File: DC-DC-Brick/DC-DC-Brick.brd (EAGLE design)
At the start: 48.3 x 73.7 mm, 20 parts

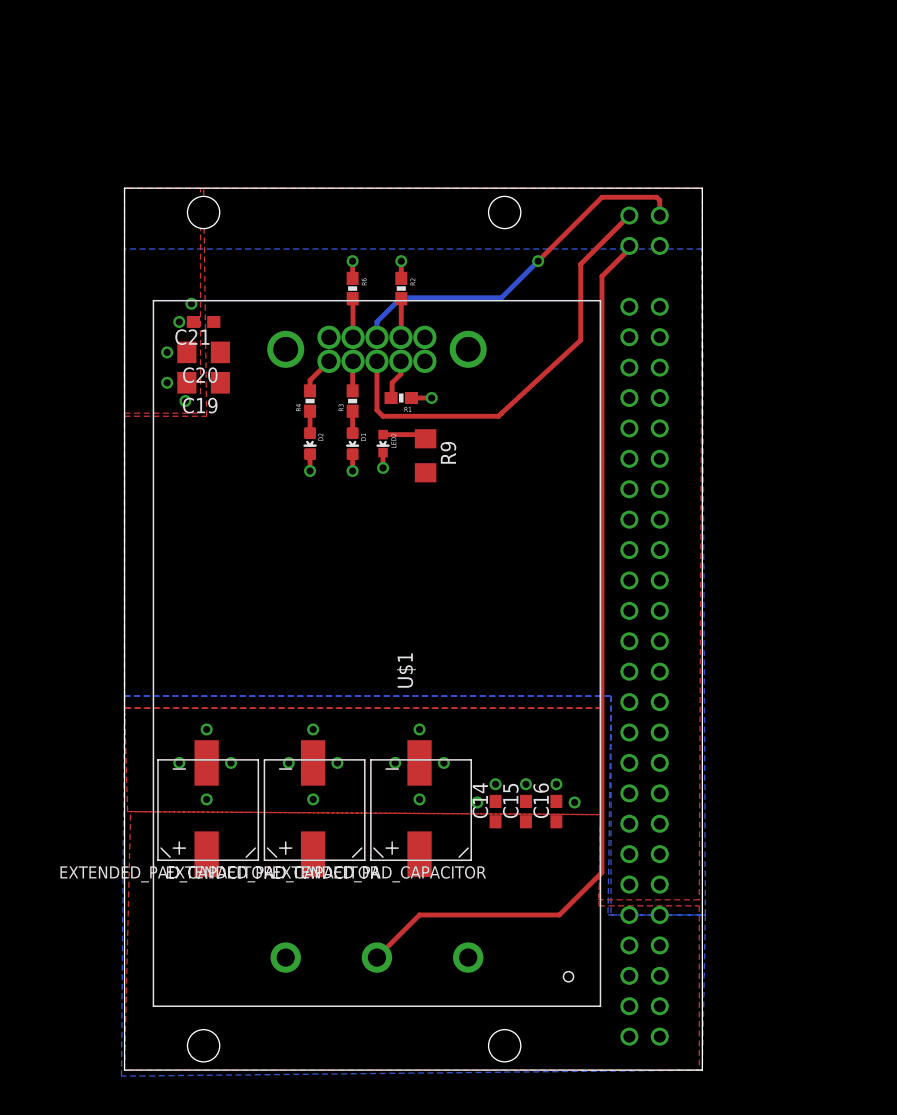
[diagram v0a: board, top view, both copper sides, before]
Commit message: Fixed some routing and added resistor
Added resistor between ON/OFF pin and V-. The resistor's value is not
necessarily the value we will end up using.
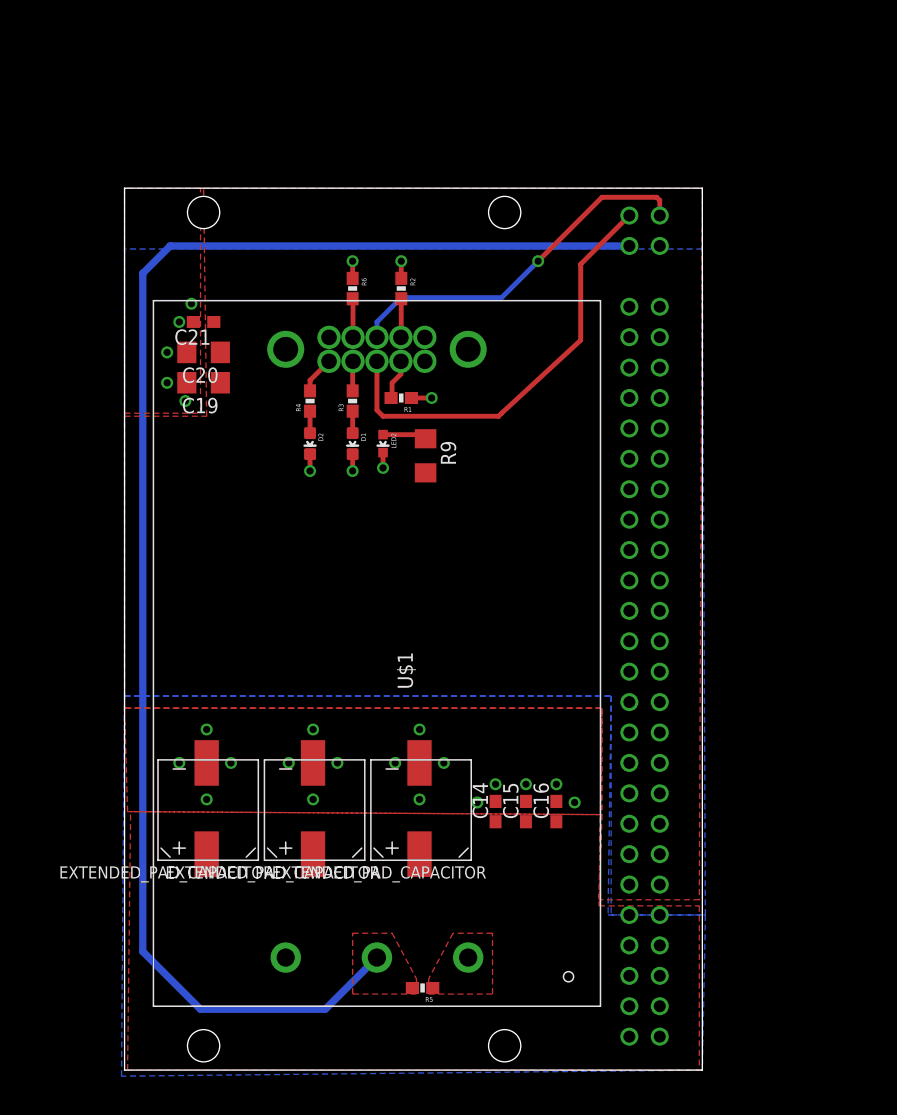
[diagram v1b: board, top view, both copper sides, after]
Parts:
- added R5: 220, SparkFun-Resistors:0603-RES
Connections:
- removed net N$9: U$1.2, U$3.P$51
- new net ON/OFF: R5.2, U$1.2, U$3.P$51
- net V-: now also R5.1
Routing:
- net ON/OFF: track 0.00 -> 121.6 mm
- net N$9: track 75.0 -> 0.00 mm
- added copper zone on layer 1, net ON/OFF
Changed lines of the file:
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@@
 <element name="U$1" library="PowerComponents" package="BRICK_DC-DC_CONVERTER" value="BRICK_DC-DC_CONVERTER" x="21.082" y="34.798" rot="R90"/>
 <element name="U$3" library="MotherboardParts" package="POWER-BRICK-CONNECTOR" value="POWER-BRICK-CONNECTOR" x="43.434" y="37.084"/>
+<element name="R5" library="SparkFun-Resistors" package="0603-RES" value="220" x="24.892" y="6.858" rot="R180">
+<attribute name="PROD_ID" value="RES-07856" x="24.892" y="6.858" size="1.778" layer="27" rot="R180" display="off"/>
+</element>
 </elements>
 <signals>
@@
 <contactref element="C22V6" pad="P$3"/>
 <contactref element="U$1" pad="1"/>
-<polygon width="0.4064" layer="1">
-<vertex x="0" y="0"/>
+<polygon width="0.4064" layer="1" rank="2">
+<vertex x="0.254" y="0"/>
 <vertex x="0.508" y="21.59"/>
 <vertex x="39.878" y="21.336"/>
@@
 <contactref element="U$3" pad="P$8"/>
 <contactref element="U$3" pad="P$9"/>
+<contactref element="R5" pad="1"/>
+<polygon width="0.6096" layer="1">
+<vertex x="27.432" y="11.43"/>
+<vertex x="25.4" y="7.62"/>
+<vertex x="25.4" y="6.35"/>
+<vertex x="30.734" y="6.35"/>
+<vertex x="30.734" y="11.43"/>
+</polygon>
 </signal>
 <signal name="N$12">
@@
 </polygon>
 </signal>
-<signal name="N$9">
+<signal name="ON/OFF">
 <contactref element="U$1" pad="2"/>
 <contactref element="U$3" pad="P$51"/>
-<wire x1="21.082" y1="9.398" x2="24.638" y2="12.954" width="0.4064" layer="1"/>
-<wire x1="24.638" y1="12.954" x2="36.322" y2="12.954" width="0.4064" layer="1"/>
-<wire x1="36.322" y1="12.954" x2="39.878" y2="16.51" width="0.4064" layer="1"/>
-<wire x1="39.878" y1="16.51" x2="39.878" y2="66.294" width="0.4064" layer="1"/>
-<wire x1="39.878" y1="66.294" x2="42.164" y2="68.58" width="0.4064" layer="1"/>
-<wire x1="42.164" y1="68.58" x2="42.164" y2="68.834" width="0.4064" layer="1"/>
+<wire x1="42.164" y1="68.834" x2="3.81" y2="68.834" width="0.6096" layer="16"/>
+<wire x1="3.81" y1="68.834" x2="1.524" y2="66.548" width="0.6096" layer="16"/>
+<wire x1="1.524" y1="66.548" x2="1.524" y2="9.906" width="0.6096" layer="16"/>
+<wire x1="1.524" y1="9.906" x2="6.35" y2="5.08" width="0.6096" layer="16"/>
+<wire x1="6.35" y1="5.08" x2="16.764" y2="5.08" width="0.6096" layer="16"/>
+<wire x1="16.764" y1="5.08" x2="21.082" y2="9.398" width="0.6096" layer="16"/>
+<contactref element="R5" pad="2"/>
+<polygon width="0.6096" layer="1">
+<vertex x="22.352" y="11.43"/>
+<vertex x="24.384" y="7.62"/>
+<vertex x="24.384" y="6.35"/>
+<vertex x="19.05" y="6.35"/>
+<vertex x="19.05" y="11.43"/>
+</polygon>
 </signal>
 <signal name="N$8">

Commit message: Worked on power polygons
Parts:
- moved C22V1 11.7 mm to (3.05, 17.5), turned to 0 degrees
- moved C22V5 11.7 mm to (11.9, 17.5), turned to 0 degrees
- moved C22V6 11.5 mm to (21.1, 17.5), turned to 0 degrees
- moved U$3 1.08 mm to (44.2, 37.8)
- turned C14 to 270 degrees
- turned C15 to 270 degrees
- turned C16 to 270 degrees
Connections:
- net V+: now also U$3.P$1, U$3.P$10, U$3.P$2, U$3.P$3, U$3.P$4, U$3.P$5, U$3.P$6, U$3.P$7, U$3.P$8, U$3.P$9; no longer U$3.P$21, U$3.P$22, U$3.P$23, U$3.P$24, U$3.P$25, U$3.P$26, U$3.P$27, U$3.P$28, U$3.P$29, U$3.P$30
- net V-: now also U$3.P$21, U$3.P$22, U$3.P$23, U$3.P$24, U$3.P$25; no longer U$3.P$10, U$3.P$6, U$3.P$7, U$3.P$8, U$3.P$9
- net VCC: now also U$3.P$26, U$3.P$27, U$3.P$28, U$3.P$29, U$3.P$30; no longer U$3.P$1, U$3.P$2, U$3.P$3, U$3.P$4, U$3.P$5
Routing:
- net V+: track 0.00 -> 112.5 mm
- net VCC: track 0.00 -> 23.3 mm
- net N$8: track 30.6 -> 9.09 mm, vias 1 -> 0
- net GND: track 8.66 -> 27.6 mm
- net ON/OFF: track 121.6 -> 122.7 mm
- net N$10: track 35.9 -> 34.9 mm
- removed copper zone on layer 1, net GND
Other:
- board size 48.3 x 73.7 mm -> 48.3 x 75.4 mm

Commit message: Updated polygons again
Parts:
- moved C22V1 36.5 mm to (34.8, 35.6), turned to 90 degrees
- moved C22V5 24.6 mm to (34.8, 26.7), turned to 90 degrees
- moved C15 18.1 mm to (30.2, 3.81), turned to 0 degrees
- moved C14 15.5 mm to (30.2, 6.10), turned to 0 degrees
- moved C16 14.4 mm to (30.2, 8.38), turned to 0 degrees
- moved C22V6 13.7 mm to (34.8, 17.8), turned to 90 degrees
- moved R5 11.4 mm to (32.0, 15.7)
- moved U$3 10.0 mm to (53.6, 41.4)
- moved C21 10.0 mm to (16.0, 66.0)
- moved D1 10.0 mm to (28.4, 55.9)
- moved D2 10.0 mm to (24.9, 55.9)
- moved LED2 10.0 mm to (31.0, 55.9)
- moved C19 10.0 mm to (16.0, 61.0)
- moved C20 10.0 mm to (16.0, 63.5)
- moved R1 10.0 mm to (32.5, 59.7)
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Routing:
- net V+: track 112.5 -> 19.7 mm, vias 0 -> 28
- net ON/OFF: track 122.7 -> 95.8 mm, vias 0 -> 1
- net N$8: track 9.09 -> 32.5 mm
- net VCC: track 23.3 -> 0.00 mm, vias 0 -> 16
- net GND: track 27.6 -> 31.6 mm
- net N$10: track 34.9 -> 34.6 mm, vias 0 -> 1
- added copper zone on layer 16, net V+
- added copper zone on layer 16, net VCC
- removed copper zone on layer 1, net ON/OFF
- removed copper zone on layer 16, net V-
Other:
- board size 48.3 x 75.4 mm -> 58.2 x 77.5 mm

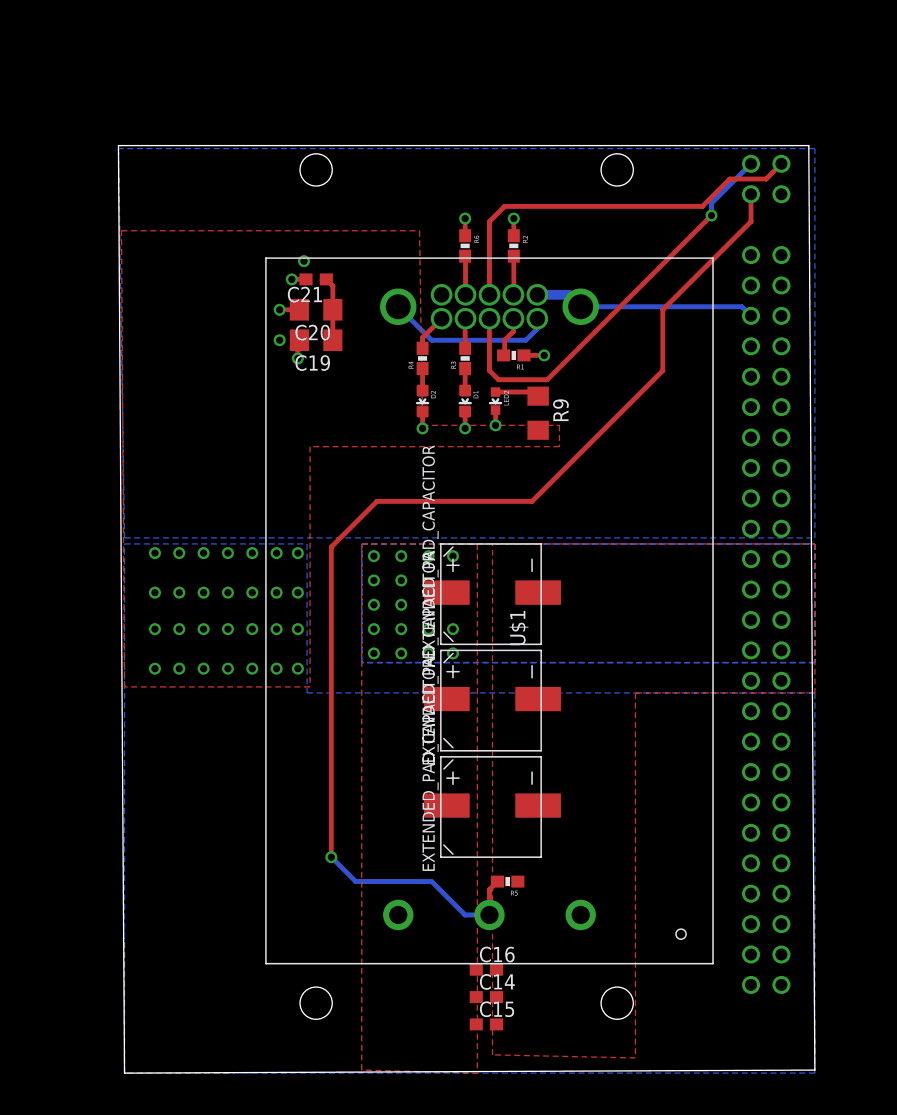
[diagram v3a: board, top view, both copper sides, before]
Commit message: cleaned up poligons
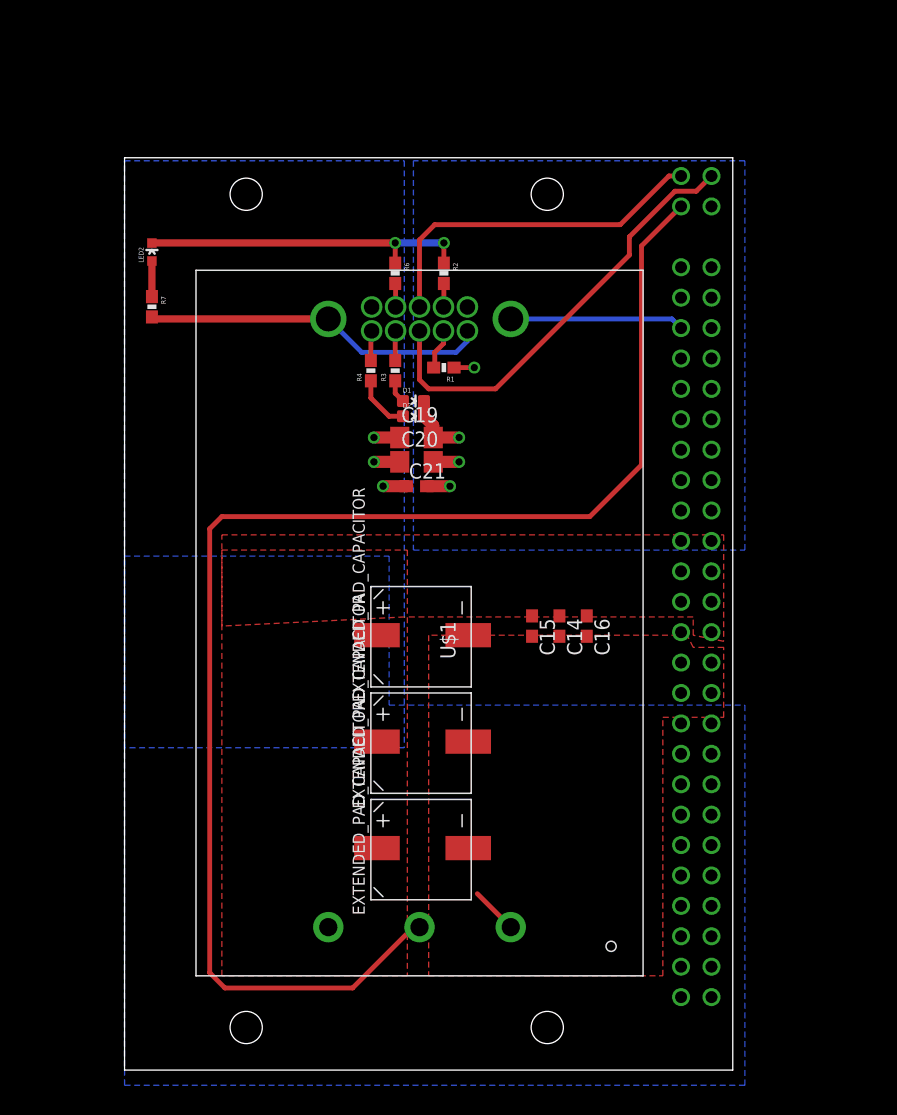
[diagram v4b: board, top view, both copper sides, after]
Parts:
- removed R5: 220, SparkFun-Resistors:0603-RES
- removed R9: 1.1k, resistor:R1206
- added R7: 470, SparkFun-Resistors:0603-RES
- moved C15 33.5 mm to (34.0, 37.1), turned to 270 degrees
- moved C14 31.6 mm to (36.3, 37.1), turned to 270 degrees
- moved LED2 31.3 mm to (2.29, 68.3), turned to 0 degrees
- moved C16 29.9 mm to (38.6, 37.1), turned to 270 degrees
- moved C21 19.2 mm to (24.4, 48.8), turned to 0 degrees
- moved C20 15.2 mm to (24.4, 50.8), turned to 0 degrees
- moved C19 11.7 mm to (24.4, 52.8), turned to 0 degrees
- moved C22V1 6.84 mm to (29.0, 32.0)
- moved C22V5 6.84 mm to (29.0, 23.1)
- moved C22V6 6.84 mm to (29.0, 14.2)
- moved R2 6.27 mm to (26.7, 66.5)
- moved R6 6.27 mm to (22.6, 66.5)
- moved R1 5.93 mm to (26.7, 58.7)
- moved R3 5.93 mm to (22.6, 58.4)
- moved U$1 5.93 mm to (24.6, 37.3)
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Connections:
- net N$10: now also U$3.P$54; no longer U$3.P$53
- net N$12: now also R7.1; no longer R9.1
- net N$8: now also U$3.P$53; no longer U$3.P$54
- net ON/OFF: no longer R5.2
- net V+: now also R7.2; no longer R9.2
- net V-: no longer R5.1
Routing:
- net ON/OFF: track 95.8 -> 118.5 mm, vias 1 -> 0
- net GND: track 31.6 -> 53.6 mm, vias 11 -> 6
- net V+: track 19.7 -> 35.2 mm, vias 28 -> 3
- net V-: track 0.00 -> 3.95 mm
- net N$5: track 1.83 -> 4.75 mm
- net N$8: track 32.5 -> 29.7 mm
- net N$10: track 34.6 -> 37.0 mm, vias 1 -> 0
- net N$1: track 3.24 -> 1.97 mm
- net N$3: track 3.24 -> 1.97 mm
- net N$12: track 3.70 -> 2.97 mm
- net N$6: track 3.13 -> 2.49 mm
- removed copper zone on layer 1, net V+
- removed copper zone on layer 16, net VCC
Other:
- board size 58.2 x 77.5 mm -> 50.8 x 76.2 mm
